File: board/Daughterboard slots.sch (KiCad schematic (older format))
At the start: 6 parts, among them P701 SLOT_A, P702 SLOT_D, P703 SLOT_B, P704 SLOT_E, P705 SLOT_C, P706 SLOT_F

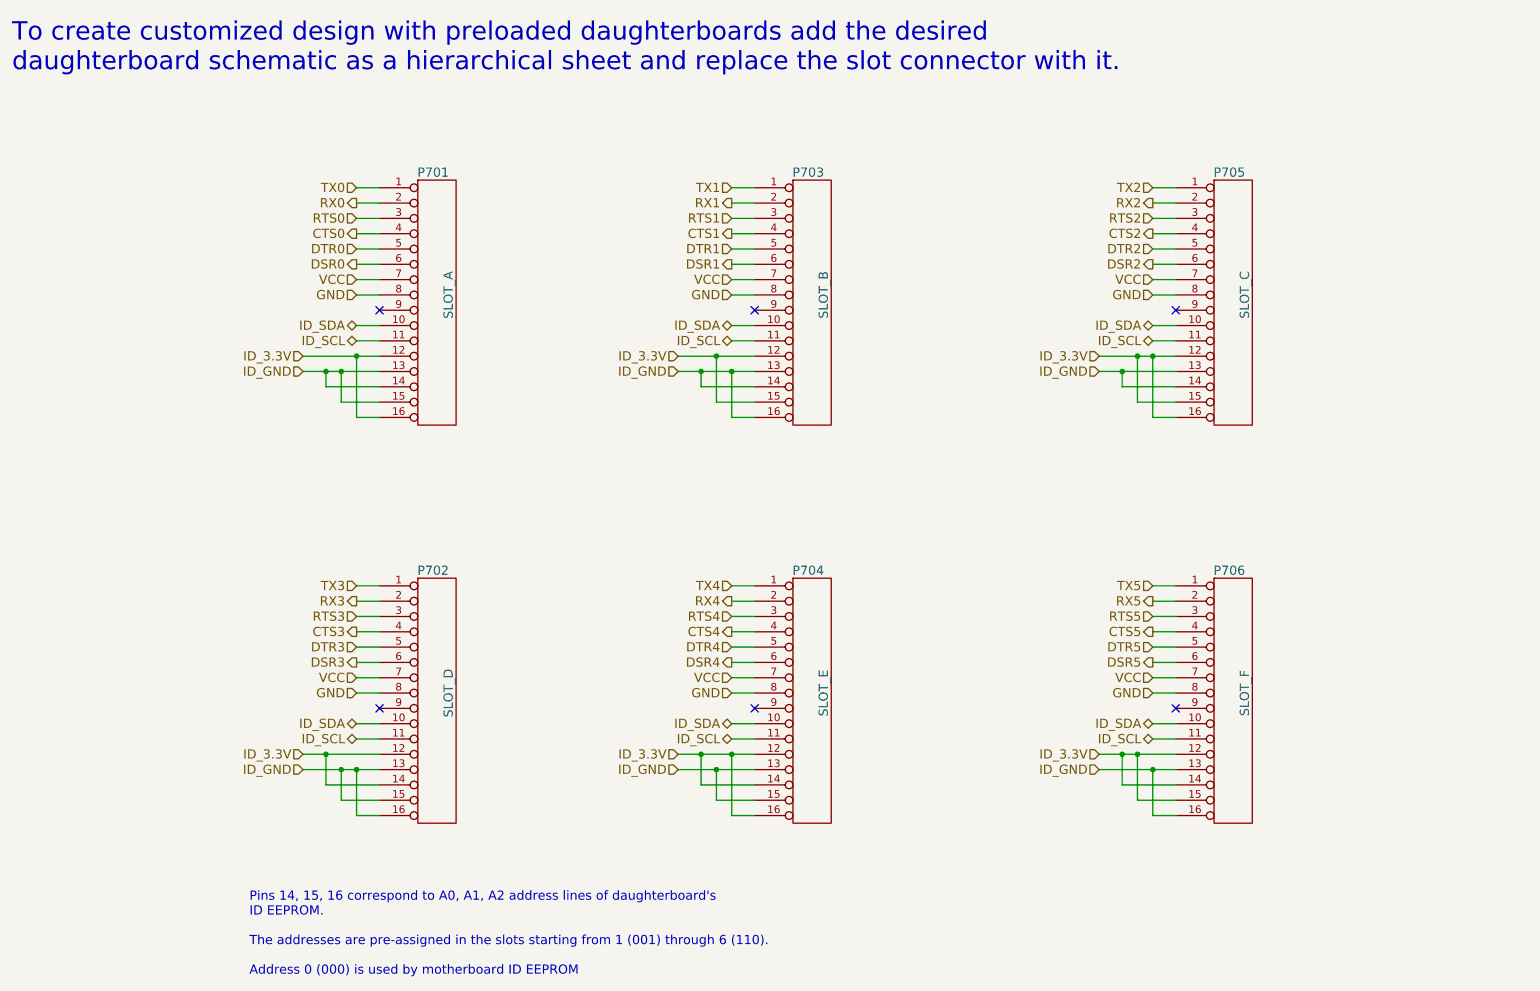
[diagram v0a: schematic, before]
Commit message: Fixed power pin and port names to include voltages
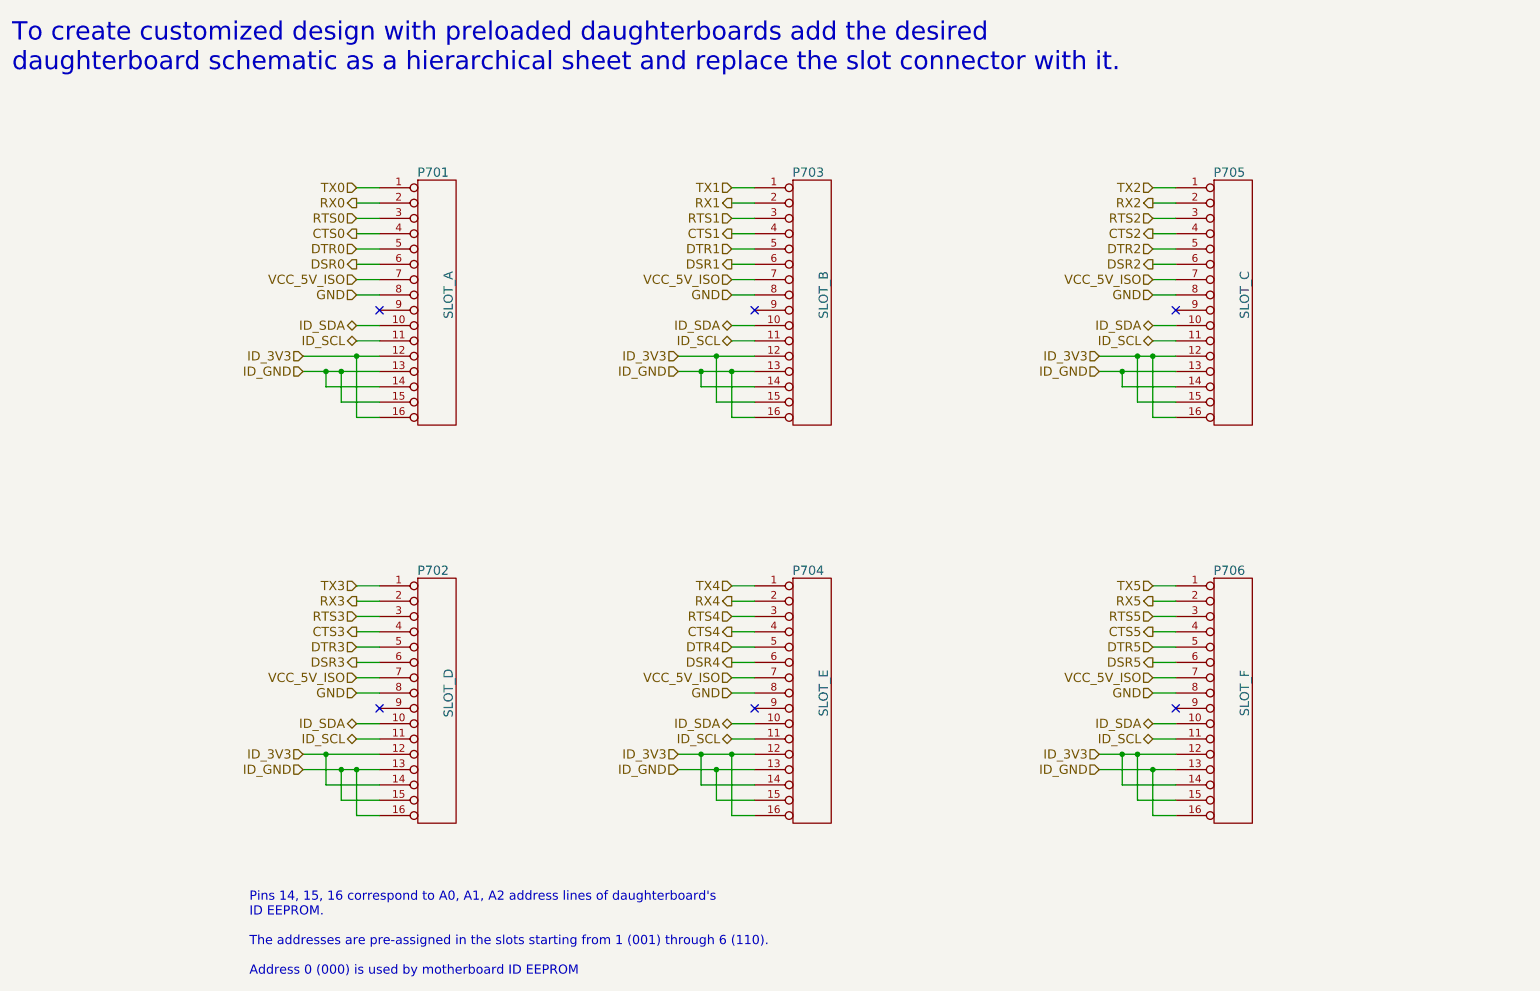
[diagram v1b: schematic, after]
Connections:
- net ID_3.3V renamed ID_3V3
- net VCC renamed VCC_5V_ISO
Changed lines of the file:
@@
 DSR0
 Text HLabel 3250 2500 0    60   Input ~ 0
-VCC
+VCC_5V_ISO
 Text HLabel 3250 2600 0    60   Input ~ 0
 GND
@@
 ID_SCL
 Text HLabel 2900 3000 0    60   Input ~ 0
-ID_3.3V
+ID_3V3
 Text HLabel 2900 3100 0    60   Input ~ 0
 ID_GND
@@
 DSR1
 Text HLabel 5700 2500 0    60   Input ~ 0
-VCC
+VCC_5V_ISO
 Text HLabel 5700 2600 0    60   Input ~ 0
 GND
@@
 DSR2
 Text HLabel 8450 2500 0    60   Input ~ 0
-VCC
+VCC_5V_ISO
 Text HLabel 8450 2600 0    60   Input ~ 0
 GND
@@
 DSR3
 Text HLabel 3250 5100 0    60   Input ~ 0
-VCC
+VCC_5V_ISO
 Text HLabel 3250 5200 0    60   Input ~ 0
 GND
@@
 DSR4
 Text HLabel 5700 5100 0    60   Input ~ 0
-VCC
+VCC_5V_ISO
 Text HLabel 5700 5200 0    60   Input ~ 0
 GND
@@
 DSR5
 Text HLabel 8450 5100 0    60   Input ~ 0
-VCC
+VCC_5V_ISO
 Text HLabel 8450 5200 0    60   Input ~ 0
 GND
@@
 ID_SCL
 Text HLabel 5350 3000 0    60   Input ~ 0
-ID_3.3V
+ID_3V3
 Text HLabel 5350 3100 0    60   Input ~ 0
 ID_GND
@@
 ID_SCL
 Text HLabel 8100 3000 0    60   Input ~ 0
-ID_3.3V
+ID_3V3
 Text HLabel 8100 3100 0    60   Input ~ 0
 ID_GND
@@
 ID_SCL
 Text HLabel 2900 5600 0    60   Input ~ 0
-ID_3.3V
+ID_3V3
 Text HLabel 2900 5700 0    60   Input ~ 0
 ID_GND
@@
 ID_SCL
 Text HLabel 5350 5600 0    60   Input ~ 0
-ID_3.3V
+ID_3V3
 Text HLabel 5350 5700 0    60   Input ~ 0
 ID_GND
@@
 ID_SCL
 Text HLabel 8100 5600 0    60   Input ~ 0
-ID_3.3V
+ID_3V3
 Text HLabel 8100 5700 0    60   Input ~ 0
 ID_GND
